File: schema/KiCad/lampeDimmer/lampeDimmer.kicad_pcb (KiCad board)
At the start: 2 copper layers, 76.5 x 46.3 mm, 21 parts, among them J1 PICkit4, J2 USART, J3 EXT_IO, J4 EXT_PWM4B, J5 EXT_PWM4D, J6 EXT_ADC1, J7 CON_POT_SW, J8 Entrée, J9 Sortie, M1 ARDUINO_MICRO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

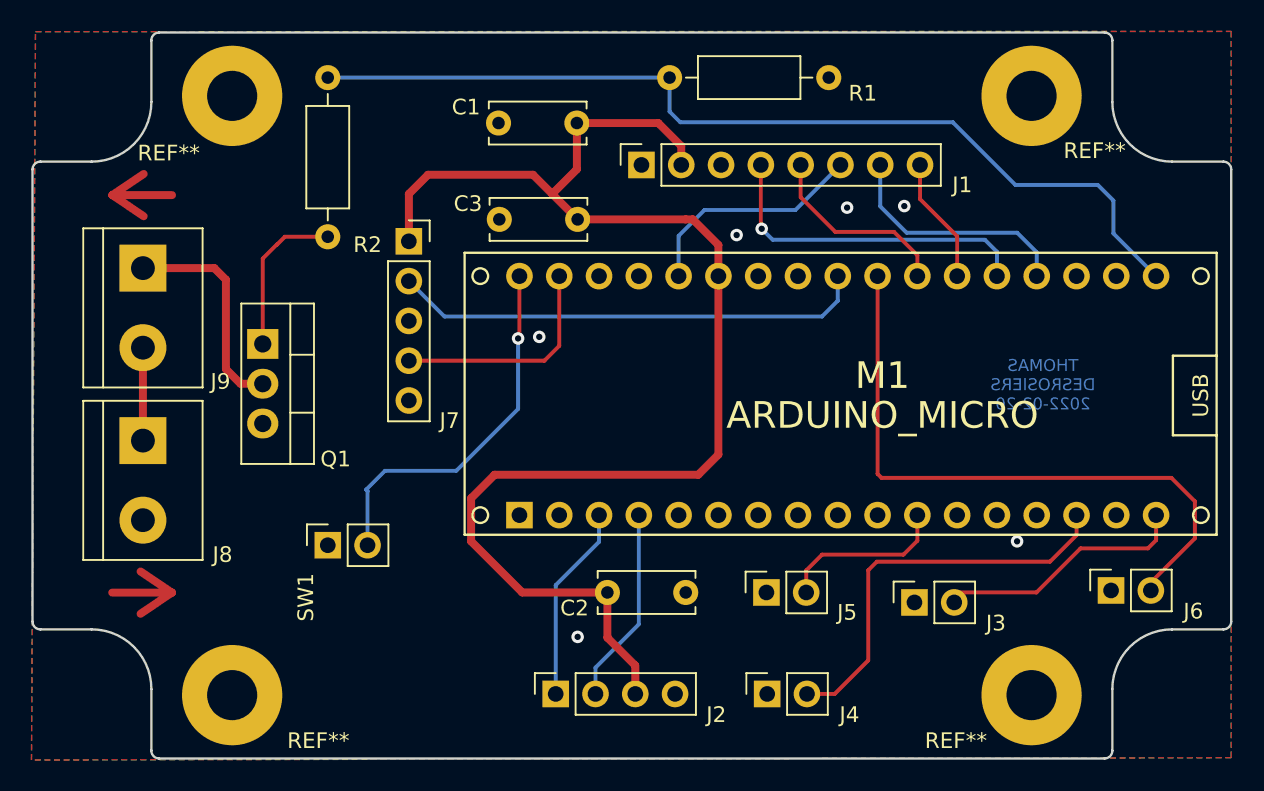
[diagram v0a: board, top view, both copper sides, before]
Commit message: [SCHÉMA + PCB]
+ Ajout de test point;
~ Traces et dégagements augmentés;
~ Rapprochement des condensateurs de découplage des composants;

+ Fichiers Gerber générés.
~ Grosseur du text augmenté.
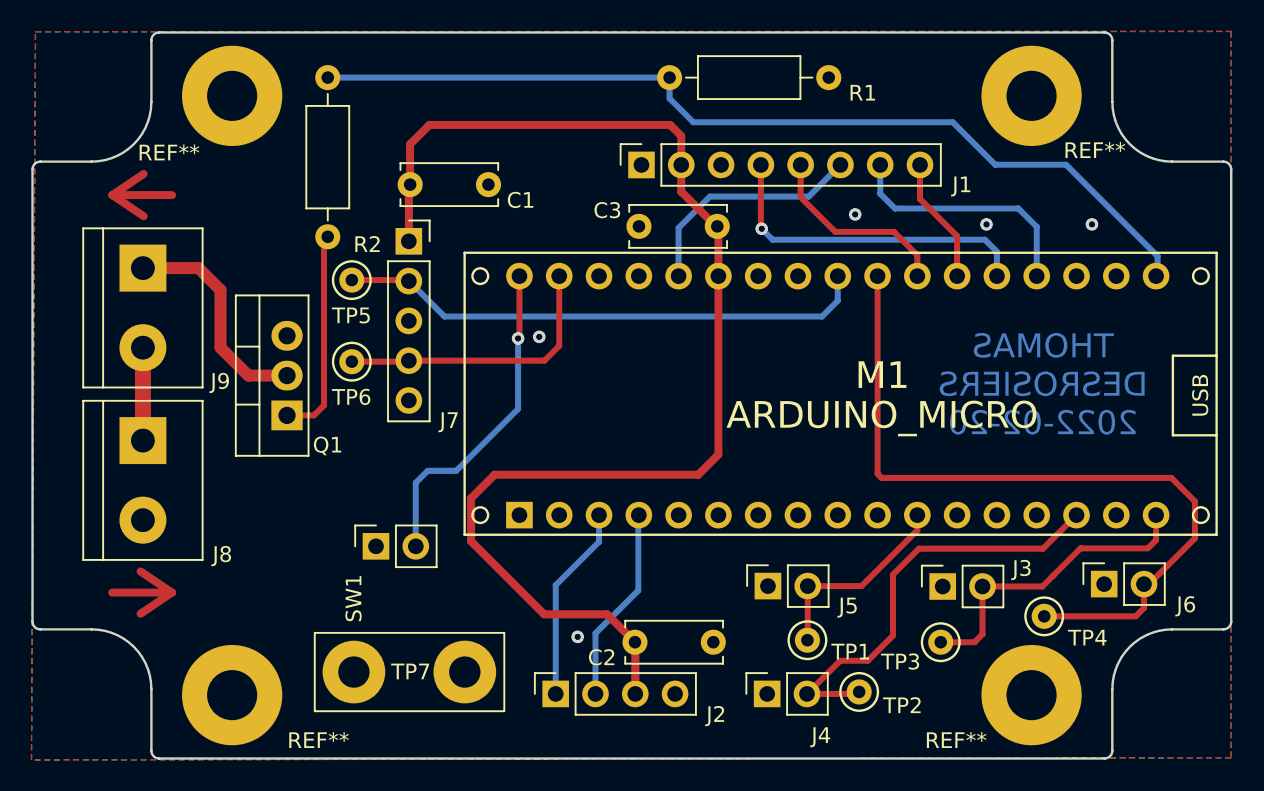
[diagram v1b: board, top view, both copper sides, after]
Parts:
- added TP1: TestPoint, THOMAS_library:TestPoint_Keystone_5000-5004_Miniature-Resistor, F.Cu at (164.7, 123.1)
- added TP2: TestPoint, THOMAS_library:TestPoint_Keystone_5000-5004_Miniature-Resistor, F.Cu at (168.0, 126.4)
- added TP3: TestPoint, THOMAS_library:TestPoint_Keystone_5000-5004_Miniature-Resistor, F.Cu at (173.2, 123.2)
- added TP4: TestPoint, THOMAS_library:TestPoint_Keystone_5000-5004_Miniature-Resistor, F.Cu at (179.8, 121.5)
- added TP5: TestPoint, THOMAS_library:TestPoint_Keystone_5000-5004_Miniature-Resistor, F.Cu at (135.6, 100.1)
- added TP6: TestPoint, THOMAS_library:TestPoint_Keystone_5000-5004_Miniature-Resistor, F.Cu at (135.6, 105.3)
- added TP7: TestPoint_2Pole, THOMAS_library:TestPoint_Bridge_Pitch7.08mm_Drill2.0mm, F.Cu at (135.8, 125.1)
- moved C1 11.3 mm to (139.4, 94.0), turned to 0 degrees
- moved C3 8.93 mm to (159.0, 96.6)
- moved Q1 4.82 mm to (131.5, 108.7), turned to 90 degrees
- moved C2 3.63 mm to (153.7, 123.2)
- moved SW1 3.08 mm to (137.2, 117.1)
- moved J3 2.07 mm to (173.4, 119.6)
- moved J6 0.60 mm to (183.7, 119.5)
- moved J5 0.42 mm to (162.2, 119.6)
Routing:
- net /EXT_ADC1: track 40.1 -> 48.2 mm
- net +5V: track 89.1 -> 81.8 mm
- net /EXT_IO: track 15.9 -> 19.8 mm
- net /POT_ADC: track 30.3 -> 34.0 mm
- net /SW_VEILLE: track 14.4 -> 18.1 mm
- net Net-(Q1-Pad1): track 10.2 -> 13.5 mm
- net Net-(M1-Pad34): track 23.9 -> 21.1 mm
- net /EXT_OC4D: track 10.9 -> 12.8 mm
- net /EXT_OC4B: track 26.0 -> 27.6 mm
- net Net-(M1-Pad18): track 60.8 -> 59.9 mm
- net GND: vias 6 -> 5

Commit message: + Ajout des fichiers gerber. + Ajout d'un fichier pdf du schéma. - Suppression du schéma sous Multisim.
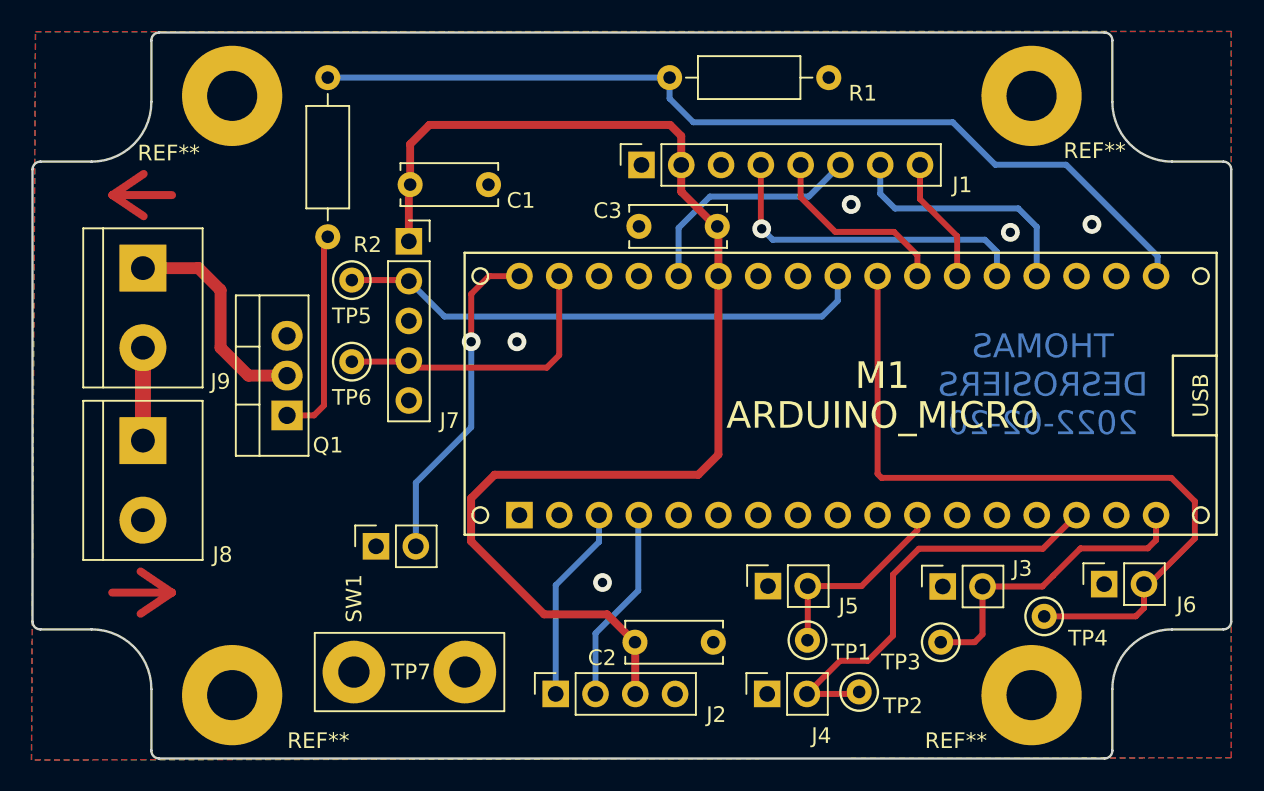
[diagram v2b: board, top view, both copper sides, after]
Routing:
- net /SW_VEILLE: track 18.1 -> 18.8 mm
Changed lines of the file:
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@@
       (drillshape 0)
       (scaleselection 1)
-      (outputdirectory "C:/Users/201770397/Desktop/KiCad/lampeDimmer/gerber/")
+      (outputdirectory "H:/Electronique/Programmation-ETC/avr/projetsPerso/Micro/lampeDimmer/schema/KiCad/lampeDimmer/gerber/")
     )
   )
@@
   (segment (start 155.956 90.17) (end 156.66499 90.87899) (width 0.508) (layer "F.Cu") (net 1))
   (segment (start 156.66499 90.87899) (end 156.66499 92.725011) (width 0.508) (layer "F.Cu") (net 1))
-  (via (at 147.6 103.7) (size 0.8) (drill 0.4) (layers "F.Cu" "B.Cu") (free) (net 2))
-  (via (at 176.149 96.52) (size 0.8) (drill 0.4) (layers "F.Cu" "B.Cu") (free) (net 2))
-  (via (at 150.049992 122.849996) (size 0.8) (drill 0.4) (layers "F.Cu" "B.Cu") (free) (net 2))
-  (via (at 182.88 96.52) (size 0.8) (drill 0.4) (layers "F.Cu" "B.Cu") (free) (net 2))
-  (via (at 167.767 95.885) (size 0.8) (drill 0.4) (layers "F.Cu" "B.Cu") (free) (net 2))
+  (via (at 146.177 104.013) (size 1.2) (drill 0.6) (layers "F.Cu" "B.Cu") (free) (net 2))
+  (via (at 151.638 119.38) (size 1.2) (drill 0.6) (layers "F.Cu" "B.Cu") (free) (net 2))
+  (via (at 177.673 97.028) (size 1.2) (drill 0.6) (layers "F.Cu" "B.Cu") (free) (net 2))
+  (via (at 182.88 96.52) (size 1.2) (drill 0.6) (layers "F.Cu" "B.Cu") (free) (net 2))
+  (via (at 167.513 95.25) (size 1.2) (drill 0.6) (layers "F.Cu" "B.Cu") (free) (net 2))
   (segment (start 179.716 119.634) (end 180.409 118.941) (width 0.381) (layer "F.Cu") (net 4))
   (segment (start 173.228 123.19) (end 175.387 123.19) (width 0.381) (layer "F.Cu") (net 4))
@@
   (segment (start 139.275 100.14) (end 139.29 100.14) (width 0.381) (layer "B.Cu") (net 8))
   (segment (start 135.636 105.283) (end 139.212 105.283) (width 0.381) (layer "F.Cu") (net 9))
-  (segment (start 139.275 105.22) (end 147.93 105.22) (width 0.381) (layer "F.Cu") (net 9))
+  (segment (start 139.719 105.664) (end 148.082 105.664) (width 0.381) (layer "F.Cu") (net 9))
   (segment (start 139.212 105.283) (end 139.275 105.22) (width 0.381) (layer "F.Cu") (net 9))
-  (segment (start 148.875503 104.274497) (end 148.875503 99.822) (width 0.381) (layer "F.Cu") (net 9))
-  (segment (start 147.93 105.22) (end 148.875503 104.274497) (width 0.381) (layer "F.Cu") (net 9))
+  (segment (start 139.275 105.22) (end 139.719 105.664) (width 0.381) (layer "F.Cu") (net 9))
+  (segment (start 148.875503 104.870497) (end 148.875503 99.822) (width 0.381) (layer "F.Cu") (net 9))
+  (segment (start 148.082 105.664) (end 148.875503 104.870497) (width 0.381) (layer "F.Cu") (net 9))
   (segment (start 122.301 104.394) (end 122.301 110.31982) (width 1.016) (layer "F.Cu") (net 10))
   (segment (start 127.254 104.394) (end 129.032 106.172) (width 0.762) (layer "F.Cu") (net 11))
@@
   (segment (start 176.71 92.71) (end 181.229 92.71) (width 0.381) (layer "B.Cu") (net 19))
   (segment (start 187.071 99.726503) (end 186.975503 99.822) (width 0.381) (layer "B.Cu") (net 19))
-  (segment (start 146.25 103.8) (end 146.335503 103.714497) (width 0.381) (layer "F.Cu") (net 20))
-  (segment (start 146.335503 103.714497) (end 146.335503 99.822) (width 0.381) (layer "F.Cu") (net 20))
-  (via (at 146.25 103.8) (size 0.8) (drill 0.4) (layers "F.Cu" "B.Cu") (net 20))
-  (segment (start 146.25 108.3) (end 142.3 112.25) (width 0.381) (layer "B.Cu") (net 20))
-  (segment (start 139.72 113.01) (end 140.48 112.25) (width 0.381) (layer "B.Cu") (net 20))
-  (segment (start 142.3 112.25) (end 140.48 112.25) (width 0.381) (layer "B.Cu") (net 20))
-  (segment (start 139.72 117.069) (end 139.72 113.01) (width 0.381) (layer "B.Cu") (net 20))
-  (segment (start 146.25 103.8) (end 146.25 108.3) (width 0.381) (layer "B.Cu") (net 20))
+  (segment (start 143.256 104.013) (end 143.256 100.965) (width 0.381) (layer "F.Cu") (net 20))
+  (segment (start 143.256 100.965) (end 144.399 99.822) (width 0.381) (layer "F.Cu") (net 20))
+  (segment (start 144.399 99.822) (end 146.335503 99.822) (width 0.381) (layer "F.Cu") (net 20))
+  (via (at 143.256 104.013) (size 1.2) (drill 0.6) (layers "F.Cu" "B.Cu") (net 20))
+  (segment (start 139.72 113.01) (end 139.72 117.069) (width 0.381) (layer "B.Cu") (net 20))
+  (segment (start 143.256 104.013) (end 143.256 109.474) (width 0.381) (layer "B.Cu") (net 20))
+  (segment (start 143.256 109.474) (end 139.72 113.01) (width 0.381) (layer "B.Cu") (net 20))
   (segment (start 166.825 92.725) (end 164.808 94.742) (width 0.381) (layer "B.Cu") (net 31))
   (segment (start 158.496 94.742) (end 156.495503 96.742497) (width 0.381) (layer "B.Cu") (net 31))
@@
   (segment (start 161.8 96.8) (end 161.745 96.745) (width 0.381) (layer "F.Cu") (net 34))
   (segment (start 161.745 96.745) (end 161.745 92.725) (width 0.381) (layer "F.Cu") (net 34))
-  (via (at 161.8 96.8) (size 0.8) (drill 0.4) (layers "F.Cu" "B.Cu") (net 34))
+  (via (at 161.8 96.8) (size 1.2) (drill 0.6) (layers "F.Cu" "B.Cu") (net 34))
   (segment (start 161.8 96.8) (end 162.5 97.5) (width 0.381) (layer "B.Cu") (net 34))
   (segment (start 176.05 97.5) (end 176.815503 98.265503) (width 0.381) (layer "B.Cu") (net 34))

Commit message: ~ Correction des erreurs de la précédente version du PCB:   - Trace sur le mauvais côté.   - Élargissement des traces.
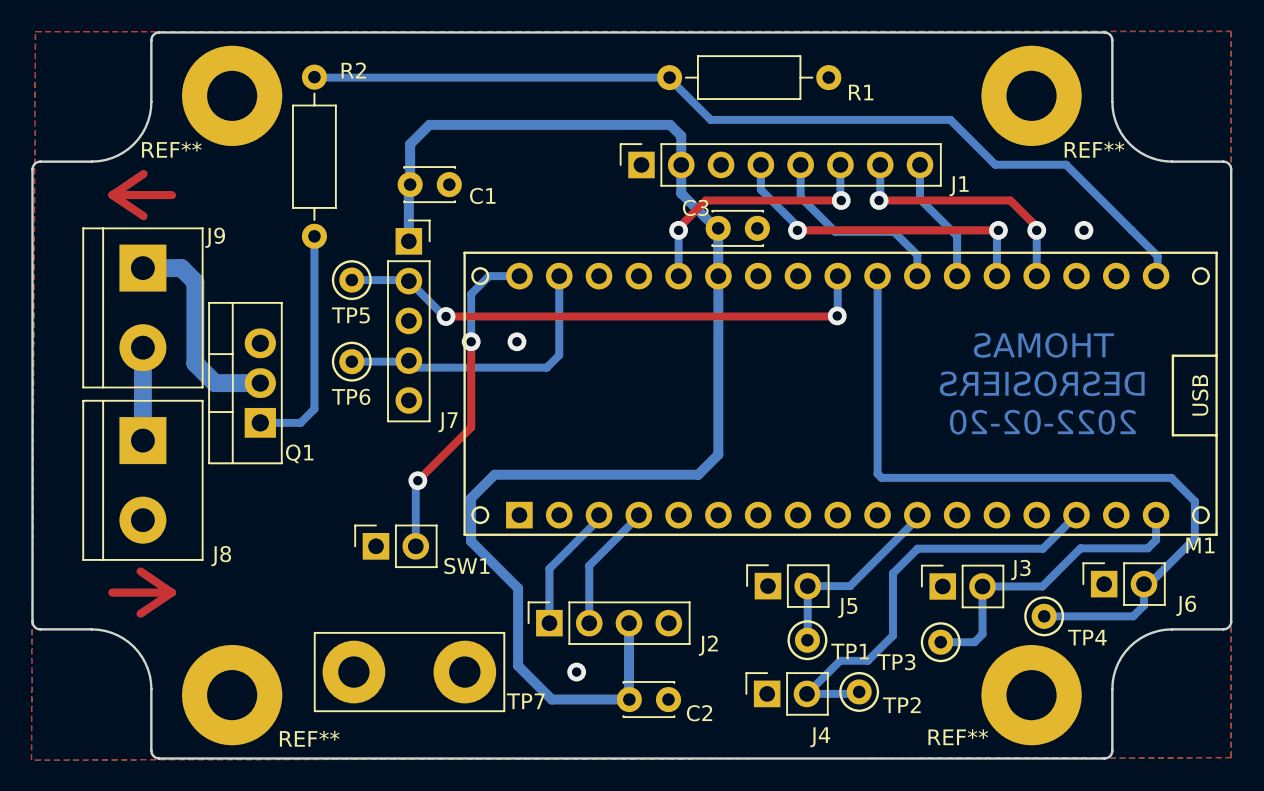
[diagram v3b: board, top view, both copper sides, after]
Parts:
- C1, C2, C3: footprint Capacitor_THT:C_Disc_D6.0mm_W2.5mm_P5.00mm -> Capacitor_THT:C_Disc_D3.0mm_W2.0mm_P2.50mm
- moved J2 4.53 mm to (148.2, 122.0)
- moved C2 3.68 mm to (153.3, 126.8)
- moved Q1 1.77 mm to (129.8, 109.2)
- moved R2 0.85 mm to (133.2, 87.1)
- moved C3 0.14 mm to (159.0, 96.8), turned to 0 degrees
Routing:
- net +5V: track 81.8 -> 87.3 mm
- net Net-(J2-Pad1): track 12.6 -> 7.95 mm
- net Net-(J2-Pad2): track 12.6 -> 8.14 mm
- net Net-(Q1-Pad1): track 13.5 -> 15.1 mm
- net Net-(J1-Pad6): track 15.1 -> 16.3 mm, vias 0 -> 2
- net /SORTIE: track 14.2 -> 13.3 mm
- net Net-(J1-Pad4): track 21.3 -> 20.7 mm, vias 1 -> 2
- net /POT_ADC: track 34.0 -> 34.4 mm, vias 0 -> 2
- net Net-(J1-Pad7): track 15.8 -> 16.2 mm, vias 0 -> 2
- net Net-(M1-Pad34): track 21.1 -> 20.9 mm, vias 1 -> 2
- net GND: vias 5 -> 3
